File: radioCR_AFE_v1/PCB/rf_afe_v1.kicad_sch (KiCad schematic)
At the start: 41 parts, among them J1 Conn_Coaxial, J2 Conn_Coaxial, U1 PHA-13LN, U3 PHA-13LN

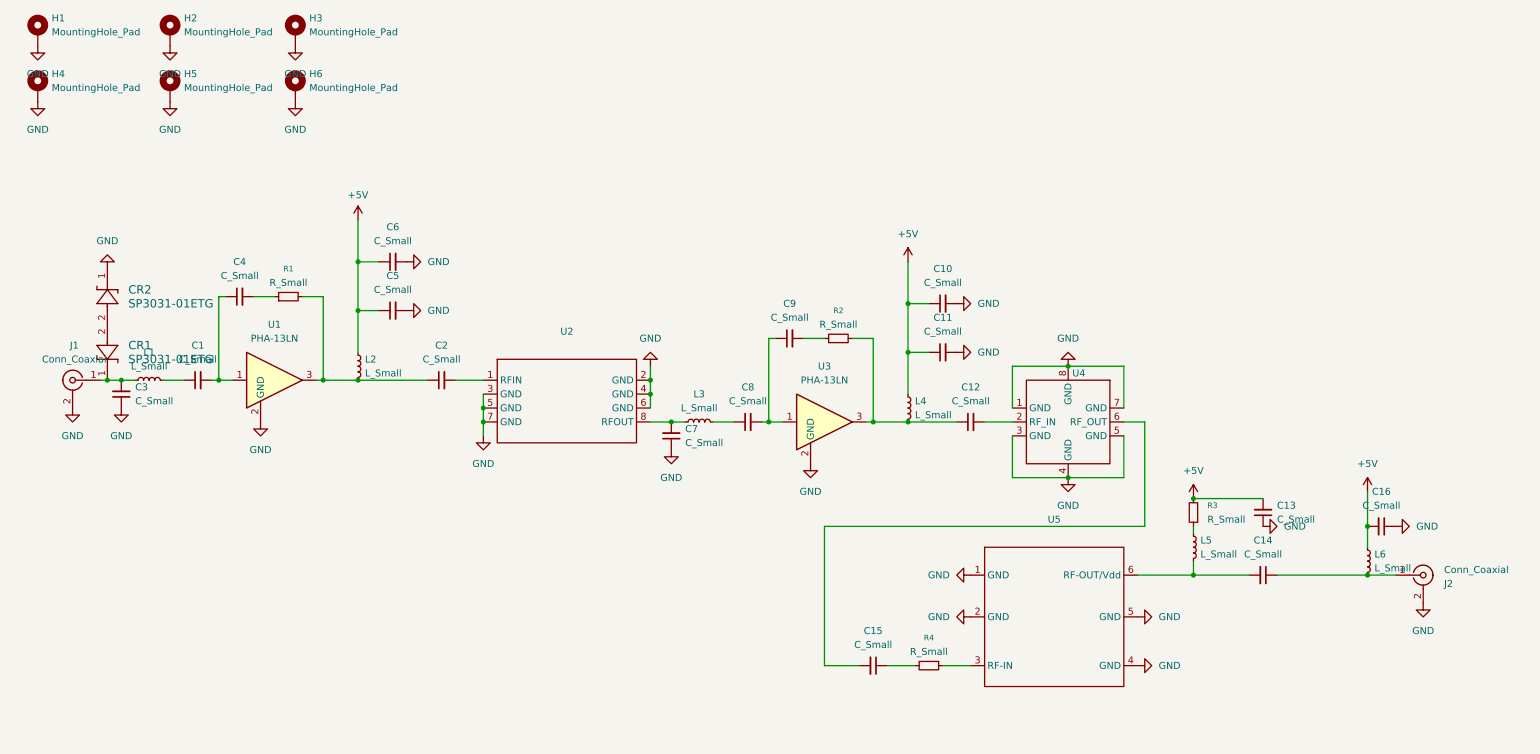
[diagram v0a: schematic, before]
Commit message: Redone according to new line-up as per matlab sims. Mask removed from board edge too!
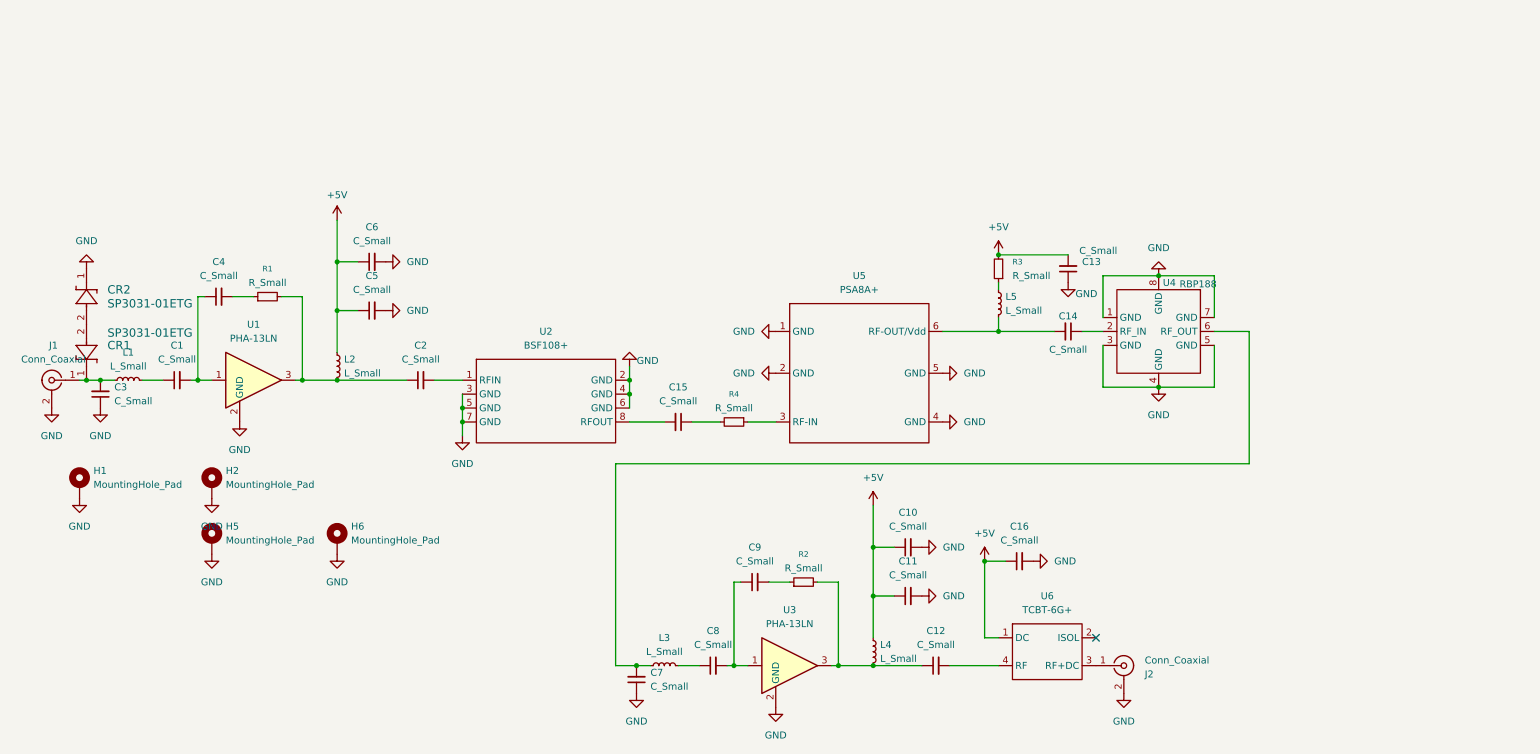
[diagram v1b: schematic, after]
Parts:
- removed H3, H4: MountingHole_Pad, MountingHole:MountingHole_3.2mm_M3_DIN965_Pad, symbol Mechanical:MountingHole_Pad
- removed L6: L_Small, Inductor_SMD:L_1210_3225Metric, symbol Device:L_Small
- added U6: TCBT-6G+, minickts_kicad:GU1604, symbol minicircuits:TCBT-6G+
- C16: footprint Capacitor_SMD:C_0805_2012Metric -> Capacitor_SMD:C_0603_1608Metric
- H1, H2, H5, H6: footprint MountingHole:MountingHole_3.2mm_M3_DIN965_Pad -> MountingHole:MountingHole_2.7mm_M2.5_Pad_Via
- U2: value ~ -> BSF108+
- U4: value ~ -> RBP188
- U5: value ~ -> PSA8A+
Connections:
- net +5V: now also C16.1, U6.1 (DC); no longer C16.2
- net GND: now also C16.2; no longer C16.1
- net at C7.2, L3.1: now also U4.6 (RF_OUT); no longer U2.8 (RFOUT)
- net at C15.2: now also U2.8 (RFOUT); no longer U4.6 (RF_OUT)
- net at J2.1 (In): now also U6.3 (RF+DC); no longer C14.1
- net at C12.2: now also U6.4 (RF); no longer U4.2 (RF_IN)
- new net: C14.1, U4.2 (RF_IN)
- no-connect marks 0 -> 1
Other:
- moved on the sheet: C1, C10, C11, C12, C13, C14, C15, C2, C3, C4, C5, C6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

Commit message: added component values
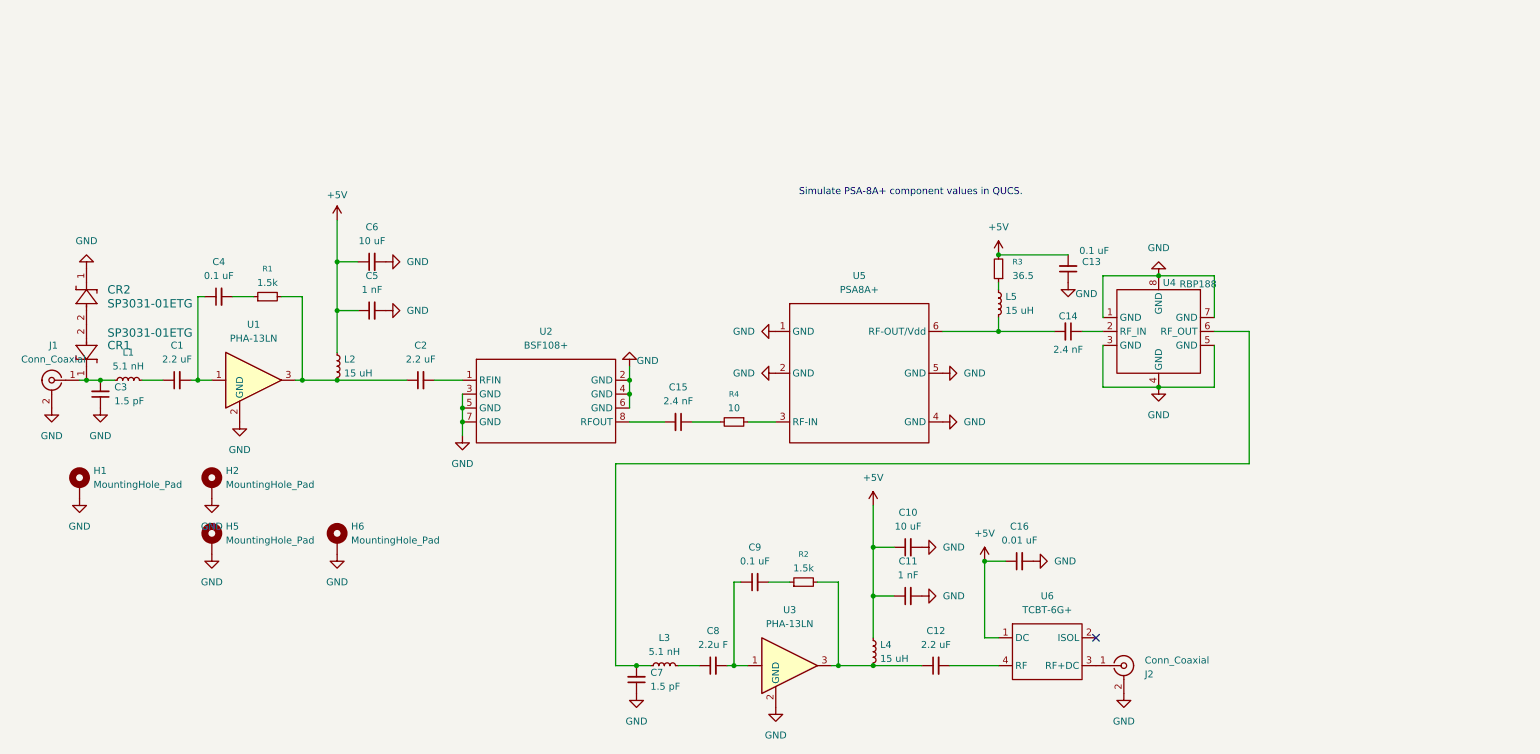
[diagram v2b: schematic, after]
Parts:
- C1, C12, C2: value C_Small -> 2.2 uF
- C10, C6: value C_Small -> 10 uF
- C11, C5: value C_Small -> 1 nF
- C13, C4, C9: value C_Small -> 0.1 uF
- C14, C15: value C_Small -> 2.4 nF
- C16: value C_Small -> 0.01 uF
- C3, C7: value C_Small -> 1.5 pF
- C8: value C_Small -> 2.2u F
- L1, L3: value L_Small -> 5.1 nH
- L2, L4, L5: value L_Small -> 15 uH
- R1, R2: value R_Small -> 1.5k
- R3: value R_Small -> 36.5
- R4: value R_Small -> 10
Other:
- note added: "Simulate PSA-8A+ component values in QUCS."
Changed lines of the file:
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@@
 	(generator_version "9.0")
 	(paper "A4")
+	(text "Simulate PSA-8A+ component values in QUCS."
+		(exclude_from_sim no)
+		(at 177.038 49.53 0)
+		(effects
+			(font
+				(size 1.27 1.27)
+			)
+		)
+	)
 	(junction
 		(at 26.67 83.82)
@@
 			)
 		)
-		(property "Value" "L_Small"
+		(property "Value" "5.1 nH"
 			(at 132.08 133.35 90)
 			(effects
@@
 			)
 		)
-		(property "Datasheet" "~"
+		(property "Datasheet" "0805HT-5N1"
 			(at 132.08 135.89 0)
 			(effects
@@
 			)
 		)
-		(property "Description" "Inductor, small symbol"
+		(property "Description" "0805HT-5N1"
 			(at 132.08 135.89 0)
 			(effects
@@
 			)
 		)
-		(property "Value" "L_Small"
+		(property "Value" "15 uH"
 			(at 171.45 134.6199 0)
 			(effects
@@
 			)
 		)
-		(property "Datasheet" "~"
+		(property "Datasheet" "LQH32DN150K53L"
 			(at 170.18 133.35 0)
 			(effects
@@
 			)
 		)
-		(property "Description" "Inductor, small symbol"
+		(property "Description" "LQH32DN150K53L"
 			(at 170.18 133.35 0)
 			(effects
@@
 			)
 		)
-		(property "Value" "C_Small"
+		(property "Value" "2.4 nF"
 			(at 134.6136 87.63 90)
 			(effects
@@
 			)
 		)
-		(property "Value" "C_Small"
+		(property "Value" "1.5 pF"
 			(at 129.54 139.6935 0)
 			(effects
@@
 			)
 		)
-		(property "Value" "C_Small"
+		(property "Value" "10 uF"
 			(at 78.7463 58.42 90)
 			(effects
@@
 			)
 		)
-		(property "Datasheet" ""
+		(property "Datasheet" "https://www.minicircuits.com/pdfs/BSF-108+.pdf"
 			(at 110.49 87.63 0)
 			(effects
@@
 			)
 		)
-		(property "Description" ""
+		(property "Description" "Band Reject filter 88 - 108 MHz"
 			(at 110.49 87.63 0)
 			(effects
@@
 			)
 		)
-		(property "Value" "C_Small"
+		(property "Value" "1 nF"
 			(at 78.7463 67.31 90)
 			(effects
@@
 			)
 		)
-		(property "Value" "C_Small"
+		(property "Value" "0.1 uF"
 			(at 148.5963 116.84 90)
 			(effects
@@
 			)
 		)
-		(property "Value" "C_Small"
+		(property "Value" "0.1 uF"
 			(at 207.772 60.198 0)
 			(effects
@@
 			)
 		)
-		(property "Value" "C_Small"
+		(property "Value" "0.01 uF"
 			(at 196.8563 113.03 90)
 			(effects
@@
 			)
 		)
-		(property "Value" "C_Small"
+		(property "Value" "2.2 uF"
 			(at 181.6163 132.08 90)
 			(effects
@@
 			)
 		)
-		(property "Value" "C_Small"
+		(property "Value" "10 uF"
 			(at 176.5363 110.49 90)
 			(effects
@@
 			)
 		)
-		(property "Value" "R_Small"
+		(property "Value" "1.5k"
 			(at 59.69 66.04 90)
 			(effects
@@
 			)
 		)
-		(property "Value" "L_Small"
+		(property "Value" "5.1 nH"
 			(at 34.29 81.28 90)
 			(effects
@@
 			)
 		)
-		(property "Datasheet" "~"
+		(property "Datasheet" "0805HT-5N1"
 			(at 34.29 83.82 0)
 			(effects
@@
 			)
 		)
-		(property "Description" "Inductor, small symbol"
+		(property "Description" "0805HT-5N1"
 			(at 34.29 83.82 0)
 			(effects
@@
 			)
 		)
-		(property "Value" "C_Small"
+		(property "Value" "2.2 uF"
 			(at 43.1863 80.01 90)
 			(effects
@@
 			)
 		)
-		(property "Value" "C_Small"
+		(property "Value" "1.5 pF"
 			(at 31.75 87.6235 0)
 			(effects
@@
 			)
 		)
-		(property "Value" "C_Small"
+		(property "Value" "0.1 uF"
 			(at 50.8063 64.77 90)
 			(effects
@@
 			)
 		)
-		(property "Value" "C_Small"
+		(property "Value" "2.4 nF"
 			(at 205.74 78.232 90)
 			(effects
@@
 			)
 		)
-		(property "Datasheet" "SP3031-01ETG"
+		(property "Datasheet" "https://www.mouser.in/ProductDetail/Littelfuse/SP3031-01ETG?qs=B%2FZyIADl9o%252B%2FfpJwZJPmLg%3D%3D"
 			(at 26.67 73.66 0)
 			(effects
@@
 			)
 		)
-		(property "Value" "C_Small"
+		(property "Value" "2.2u F"
 			(at 140.9763 132.08 90)
 			(effects
@@
 			)
 		)
-		(property "Datasheet" ""
+		(property "Datasheet" "https://www.minicircuits.com/pdfs/RBP-188+.pdf"
 			(at 222.25 74.93 0)
 			(effects
@@
 			)
 		)
-		(property "Description" ""
+		(property "Description" "Band pass filter 138 - 250 MHz"
 			(at 222.25 74.93 0)
 			(effects
@@
 			)
 		)
-		(property "Value" "R_Small"
+		(property "Value" "36.5"
 			(at 195.58 64.7699 0)
 			(effects
@@
 			)
 		)
-		(property "Value" "C_Small"
+		(property "Value" "2.2 uF"
 			(at 87.6363 80.01 90)
 			(effects
@@
 			)
 		)
-		(property "Value" "R_Small"
+		(property "Value" "10"
 			(at 144.78 88.9 90)
 			(effects
@@
 			)
 		)
-		(property "Value" "L_Small"
+		(property "Value" "15 uH"
 			(at 194.31 71.1199 0)
 			(effects
@@
 			)
 		)
-		(property "Datasheet" "~"
+		(property "Datasheet" "LQH32DN150K53L"
 			(at 193.04 69.85 0)
 			(effects
@@
 			)
 		)
-		(property "Description" "Inductor, small symbol"
+		(property "Description" "LQH32DN150K53L"
 			(at 193.04 69.85 0)
 			(effects
@@
 			)
 		)
-		(property "Datasheet" ""
+		(property "Datasheet" "https://www.minicircuits.com/pdfs/PSA-8A+.pdf"
 			(at 167.64 82.55 0)
 			(effects
@@
 			)
 		)
-		(property "Description" ""
+		(property "Description" "Amplifier Gaom block"
 			(at 167.64 82.55 0)
 			(effects
@@
 			)
 		)
-		(property "Value" "R_Small"
+		(property "Value" "1.5k"
 			(at 157.48 118.11 90)
 			(effects
@@
 			)
 		)
-		(property "Value" "C_Small"
+		(property "Value" "1 nF"
 			(at 176.5363 119.38 90)
 			(effects
@@
 			)
 		)
-		(property "Datasheet" "SP3031-01ETG"
+		(property "Datasheet" "https://www.mouser.in/ProductDetail/Littelfuse/SP3031-01ETG?qs=B%2FZyIADl9o%252B%2FfpJwZJPmLg%3D%3D"
 			(at 26.67 73.66 0)
 			(effects
@@
 			)
 		)
-		(property "Value" "L_Small"
+		(property "Value" "15 uH"
 			(at 73.66 82.5499 0)
 			(effects
@@
 			)
 		)
-		(property "Datasheet" "~"
+		(property "Datasheet" "LQH32DN150K53L"
 			(at 72.39 81.28 0)
 			(effects
@@
 			)
 		)
-		(property "Description" "Inductor, small symbol"
+		(property "Description" "LQH32DN150K53L"
 			(at 72.39 81.28 0)
 			(effects
@@
 			)
 		)
-		(property "Datasheet" ""
+		(property "Datasheet" "https://www.minicircuits.com/pdfs/TCBT-6G+.pdf"
 			(at 201.93 133.35 0)
 			(effects
@@
 			)
 		)
-		(property "Description" ""
+		(property "Description" "TCBT-6G+"
 			(at 201.93 133.35 0)
 			(effects
